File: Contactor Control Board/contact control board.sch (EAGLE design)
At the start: 29 parts, among them K1 DS2Y-S-DC5V, Q1 2n2222, Q3 2n2222, Q4 MOSFET-NCHANNELFQP30N06L, U1 LM393AN

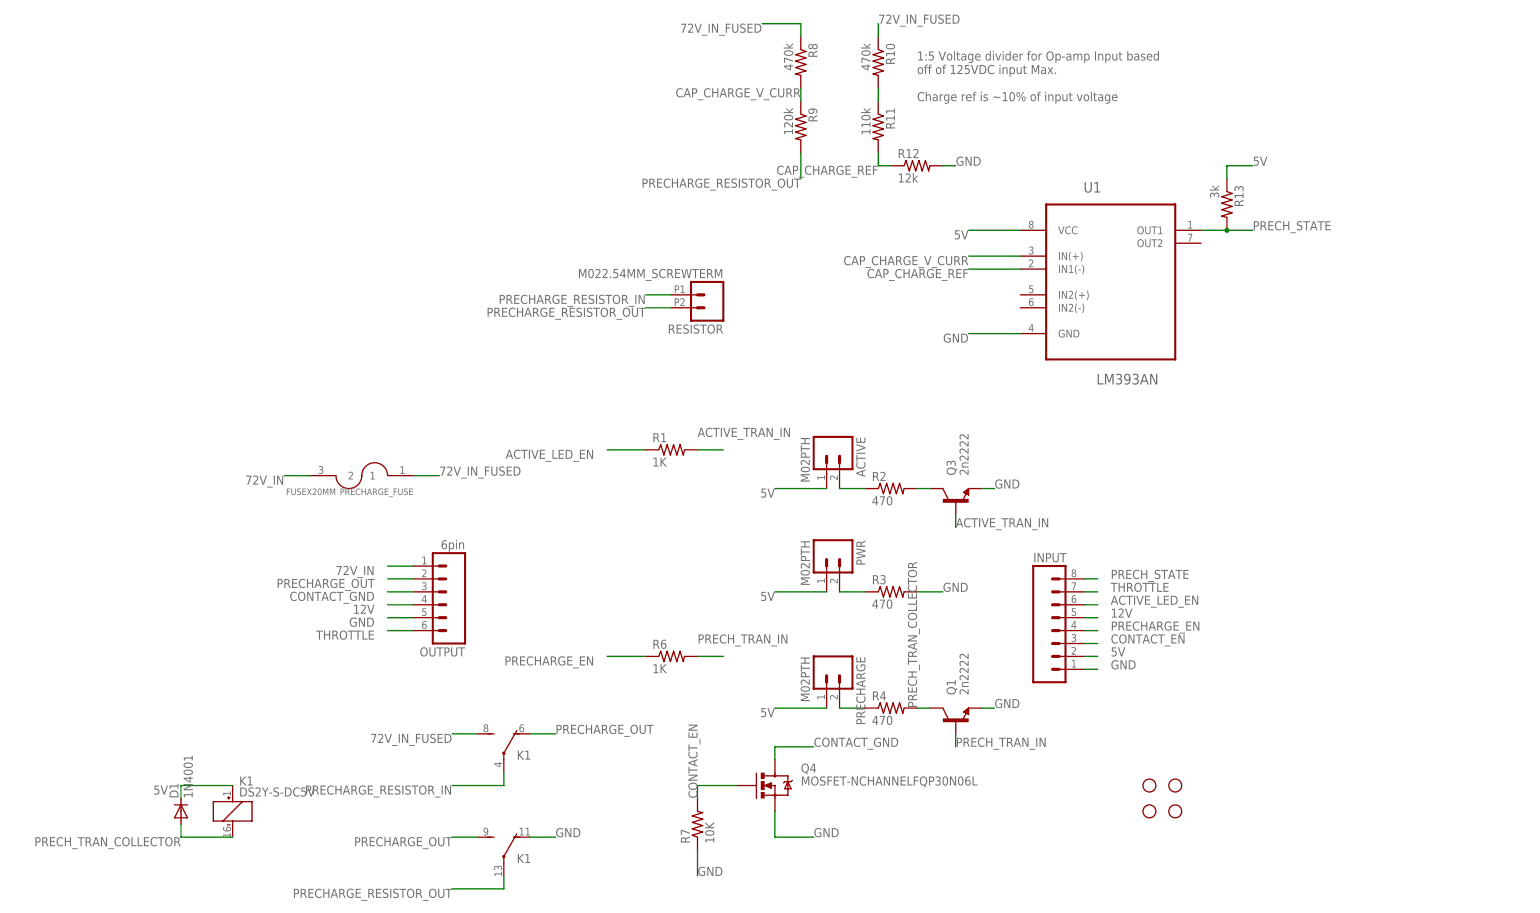
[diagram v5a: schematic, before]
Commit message: Simplified board by removing power LED pin, it's just run from 5V now.
Swapped pins in the voltage comparator to produce a HIGH output when the
capacitor voltage drops below the reference voltage (instead of vice
versa).
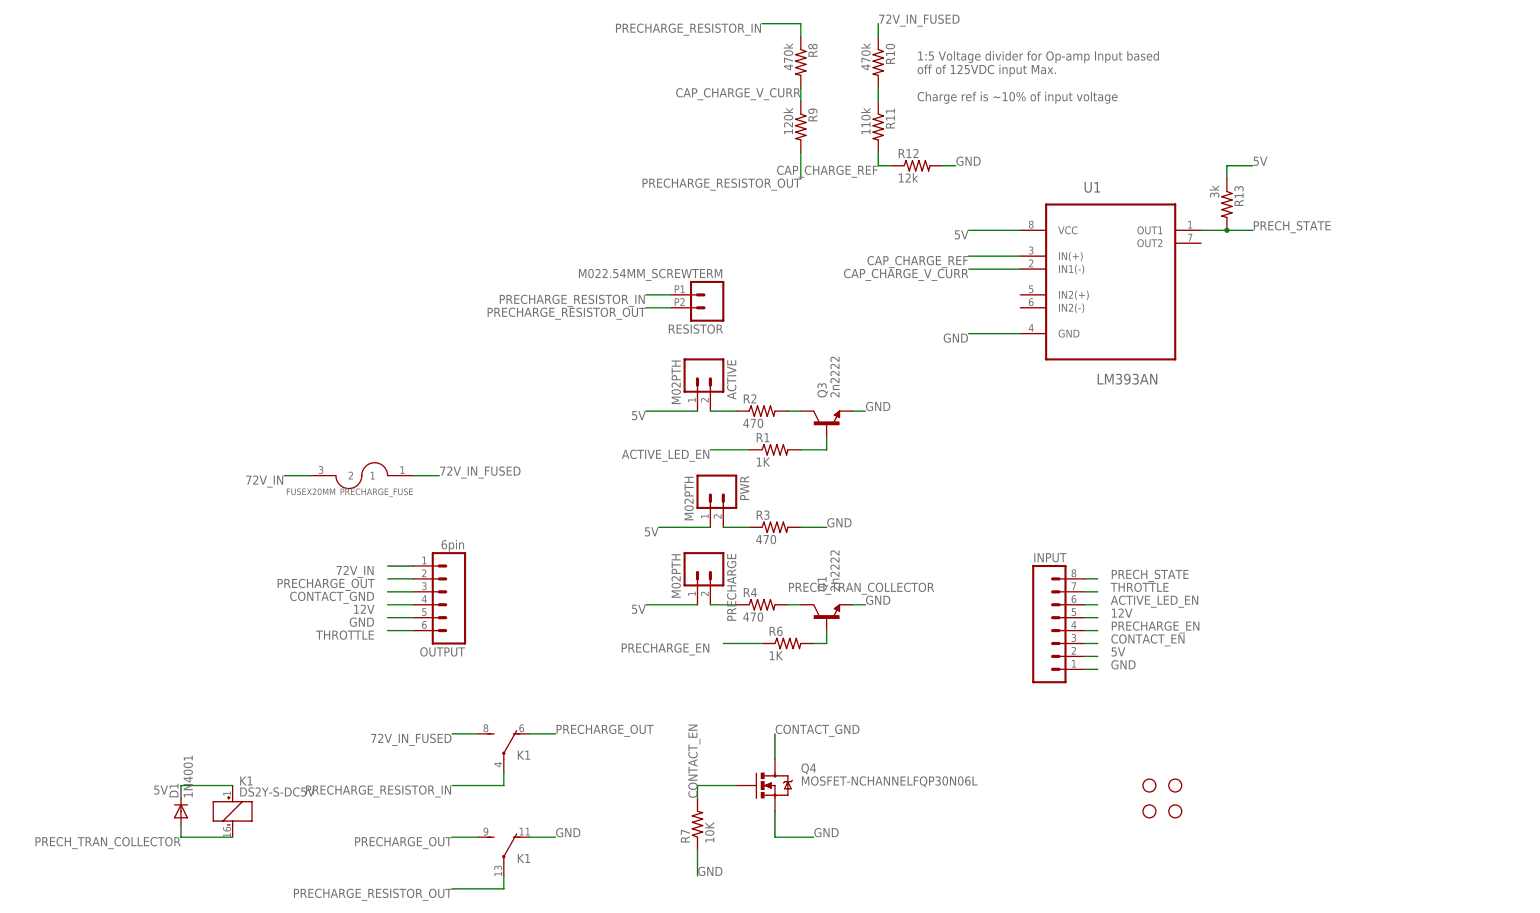
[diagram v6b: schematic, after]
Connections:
- net ACTIVE_TRAN_IN renamed N$2
- net 72V_IN_FUSED: no longer R8.1
- net CAP_CHARGE_REF: now also U1.IN(+); no longer U1.IN1(-)
- net CAP_CHARGE_V_CURR: now also U1.IN1(-); no longer U1.IN(+)
- net PRECHARGE_RESISTOR_IN: now also R8.1
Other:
- moved on the sheet: ACTIVE, PRECHARGE, PWR, Q1, Q3, R1, R2, R3, R4, R6
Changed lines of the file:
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@@
 </plain>
 <instances>
-<instance part="R1" gate="G$1" x="45.72" y="83.82"/>
-<instance part="R2" gate="G$1" x="88.9" y="76.2"/>
-<instance part="R3" gate="G$1" x="88.9" y="55.88"/>
-<instance part="R4" gate="G$1" x="88.9" y="33.02"/>
-<instance part="R6" gate="G$1" x="45.72" y="43.18"/>
+<instance part="R1" gate="G$1" x="66.04" y="83.82"/>
+<instance part="R2" gate="G$1" x="63.5" y="91.44"/>
+<instance part="R3" gate="G$1" x="66.04" y="68.58"/>
+<instance part="R4" gate="G$1" x="63.5" y="53.34"/>
+<instance part="R6" gate="G$1" x="68.58" y="45.72"/>
 <instance part="R7" gate="G$1" x="50.8" y="10.16" rot="R90"/>
 <instance part="Q4" gate="G$1" x="66.04" y="17.78"/>
@@
 <instance part="STANDOFF4" gate="G$1" x="139.7" y="12.7"/>
 <instance part="PRECHARGE_FUSE" gate="G$1" x="-15.24" y="78.74" rot="R180"/>
-<instance part="ACTIVE" gate="G$1" x="76.2" y="83.82" rot="R270"/>
-<instance part="PWR" gate="G$1" x="76.2" y="63.5" rot="R270"/>
-<instance part="PRECHARGE" gate="G$1" x="76.2" y="40.64" rot="R270"/>
-<instance part="Q1" gate="G$1" x="101.6" y="30.48" rot="R90"/>
-<instance part="Q3" gate="G$1" x="101.6" y="73.66" rot="R90"/>
+<instance part="ACTIVE" gate="G$1" x="50.8" y="99.06" rot="R270"/>
+<instance part="PWR" gate="G$1" x="53.34" y="76.2" rot="R270"/>
+<instance part="PRECHARGE" gate="G$1" x="50.8" y="60.96" rot="R270"/>
+<instance part="Q1" gate="G$1" x="76.2" y="50.8" rot="R90"/>
+<instance part="Q3" gate="G$1" x="76.2" y="88.9" rot="R90"/>
 <instance part="RESISTOR" gate="G$1" x="53.34" y="114.3" rot="R180"/>
 <instance part="R8" gate="G$1" x="71.12" y="160.02" rot="R270"/>
@@
 </segment>
 <segment>
-<wire x1="66.04" y1="76.2" x2="76.2" y2="76.2" width="0.2032" layer="91"/>
+<wire x1="40.64" y1="91.44" x2="50.8" y2="91.44" width="0.2032" layer="91"/>
 <pinref part="ACTIVE" gate="G$1" pin="1"/>
-<label x="66.04" y="76.2" size="1.778" layer="95" rot="R180"/>
+<label x="40.64" y="91.44" size="1.778" layer="95" rot="R180"/>
 </segment>
 <segment>
 <pinref part="PWR" gate="G$1" pin="1"/>
-<wire x1="76.2" y1="55.88" x2="66.04" y2="55.88" width="0.2032" layer="91"/>
-<label x="66.04" y="55.88" size="1.778" layer="95" rot="R180"/>
+<wire x1="53.34" y1="68.58" x2="43.18" y2="68.58" width="0.2032" layer="91"/>
+<label x="43.18" y="68.58" size="1.778" layer="95" rot="R180"/>
 </segment>
 <segment>
 <pinref part="PRECHARGE" gate="G$1" pin="1"/>
-<wire x1="76.2" y1="33.02" x2="66.04" y2="33.02" width="0.2032" layer="91"/>
-<label x="66.04" y="33.02" size="1.778" layer="95" rot="R180"/>
+<wire x1="50.8" y1="53.34" x2="40.64" y2="53.34" width="0.2032" layer="91"/>
+<label x="40.64" y="53.34" size="1.778" layer="95" rot="R180"/>
 </segment>
 <segment>
@@
 <segment>
 <pinref part="Q1" gate="G$1" pin="E"/>
-<wire x1="106.68" y1="33.02" x2="109.22" y2="33.02" width="0.2032" layer="91"/>
-<label x="109.22" y="33.02" size="1.778" layer="95"/>
+<wire x1="81.28" y1="53.34" x2="83.82" y2="53.34" width="0.2032" layer="91"/>
+<label x="83.82" y="53.34" size="1.778" layer="95"/>
 </segment>
 <segment>
 <pinref part="Q3" gate="G$1" pin="E"/>
-<wire x1="106.68" y1="76.2" x2="109.22" y2="76.2" width="0.2032" layer="91"/>
-<label x="109.22" y="76.2" size="1.778" layer="95"/>
+<wire x1="81.28" y1="91.44" x2="83.82" y2="91.44" width="0.2032" layer="91"/>
+<label x="83.82" y="91.44" size="1.778" layer="95"/>
 </segment>
 <segment>
@@
 <segment>
 <pinref part="R3" gate="G$1" pin="2"/>
-<wire x1="93.98" y1="55.88" x2="99.06" y2="55.88" width="0.2032" layer="91"/>
-<label x="99.06" y="55.88" size="1.778" layer="95"/>
+<wire x1="71.12" y1="68.58" x2="76.2" y2="68.58" width="0.2032" layer="91"/>
+<label x="76.2" y="68.58" size="1.778" layer="95"/>
 </segment>
 </net>
@@
 <segment>
 <pinref part="R6" gate="G$1" pin="1"/>
-<wire x1="40.64" y1="43.18" x2="33.02" y2="43.18" width="0.2032" layer="91"/>
-<label x="30.48" y="43.18" size="1.778" layer="95" rot="R180"/>
+<wire x1="63.5" y1="45.72" x2="55.88" y2="45.72" width="0.2032" layer="91"/>
+<label x="53.34" y="45.72" size="1.778" layer="95" rot="R180"/>
 </segment>
 <segment>
@@
 <segment>
 <pinref part="R1" gate="G$1" pin="1"/>
-<wire x1="40.64" y1="83.82" x2="33.02" y2="83.82" width="0.2032" layer="91"/>
-<label x="30.48" y="83.82" size="1.778" layer="95" rot="R180"/>
+<wire x1="60.96" y1="83.82" x2="53.34" y2="83.82" width="0.2032" layer="91"/>
+<label x="53.34" y="83.82" size="1.778" layer="95" rot="R180"/>
 </segment>
 </net>
@@
 <pinref part="R2" gate="G$1" pin="1"/>
 <pinref part="ACTIVE" gate="G$1" pin="2"/>
-<wire x1="78.74" y1="76.2" x2="83.82" y2="76.2" width="0.2032" layer="91"/>
+<wire x1="53.34" y1="91.44" x2="58.42" y2="91.44" width="0.2032" layer="91"/>
 </segment>
 </net>
@@
 <pinref part="R3" gate="G$1" pin="1"/>
 <pinref part="PWR" gate="G$1" pin="2"/>
-<wire x1="78.74" y1="55.88" x2="83.82" y2="55.88" width="0.2032" layer="91"/>
+<wire x1="55.88" y1="68.58" x2="60.96" y2="68.58" width="0.2032" layer="91"/>
 </segment>
 </net>
@@
 <pinref part="R4" gate="G$1" pin="1"/>
 <pinref part="PRECHARGE" gate="G$1" pin="2"/>
-<wire x1="78.74" y1="33.02" x2="83.82" y2="33.02" width="0.2032" layer="91"/>
+<wire x1="53.34" y1="53.34" x2="58.42" y2="53.34" width="0.2032" layer="91"/>
 </segment>
 </net>
@@
 </segment>
 <segment>
-<pinref part="R8" gate="G$1" pin="1"/>
-<wire x1="71.12" y1="165.1" x2="71.12" y2="167.64" width="0.2032" layer="91"/>
-<wire x1="71.12" y1="167.64" x2="63.5" y2="167.64" width="0.2032" layer="91"/>
-<label x="63.5" y="167.64" size="1.778" layer="95" rot="R180"/>
-</segment>
-<segment>
 <pinref part="K1" gate="2" pin="S"/>
 <wire x1="7.62" y1="27.94" x2="2.54" y2="27.94" width="0.2032" layer="91"/>
@@
 <segment>
 <pinref part="Q4" gate="G$1" pin="D"/>
-<wire x1="66.04" y1="22.86" x2="66.04" y2="25.4" width="0.2032" layer="91"/>
-<wire x1="66.04" y1="25.4" x2="73.66" y2="25.4" width="0.2032" layer="91"/>
-<label x="73.66" y="25.4" size="1.778" layer="95"/>
-</segment>
-</net>
-<net name="ACTIVE_TRAN_IN" class="0">
-<segment>
-<pinref part="R1" gate="G$1" pin="2"/>
-<wire x1="50.8" y1="83.82" x2="55.88" y2="83.82" width="0.2032" layer="91"/>
-<label x="50.8" y="86.36" size="1.778" layer="95"/>
-</segment>
-<segment>
-<wire x1="101.6" y1="71.12" x2="101.6" y2="68.58" width="0.2032" layer="91"/>
-<label x="101.6" y="68.58" size="1.778" layer="95"/>
-<pinref part="Q3" gate="G$1" pin="B"/>
-</segment>
-</net>
-<net name="PRECH_TRAN_IN" class="0">
-<segment>
-<pinref part="R6" gate="G$1" pin="2"/>
-<wire x1="50.8" y1="43.18" x2="55.88" y2="43.18" width="0.2032" layer="91"/>
-<label x="50.8" y="45.72" size="1.778" layer="95"/>
-</segment>
-<segment>
-<wire x1="101.6" y1="27.94" x2="101.6" y2="25.4" width="0.2032" layer="91"/>
-<label x="101.6" y="25.4" size="1.778" layer="95"/>
-<pinref part="Q1" gate="G$1" pin="B"/>
+<wire x1="66.04" y1="22.86" x2="66.04" y2="27.94" width="0.2032" layer="91"/>
+<label x="66.04" y="27.94" size="1.778" layer="95"/>
 </segment>
 </net>
@@
 <segment>
 <pinref part="R2" gate="G$1" pin="2"/>
-<wire x1="96.52" y1="76.2" x2="93.98" y2="76.2" width="0.1524" layer="91"/>
+<wire x1="71.12" y1="91.44" x2="68.58" y2="91.44" width="0.1524" layer="91"/>
 <pinref part="Q3" gate="G$1" pin="C"/>
 </segment>
@@
 <segment>
 <pinref part="R4" gate="G$1" pin="2"/>
-<wire x1="96.52" y1="33.02" x2="93.98" y2="33.02" width="0.1524" layer="91"/>
-<label x="93.98" y="33.02" size="1.778" layer="95" rot="R90"/>
+<wire x1="71.12" y1="53.34" x2="68.58" y2="53.34" width="0.1524" layer="91"/>
+<label x="68.58" y="55.88" size="1.778" layer="95"/>
 <pinref part="Q1" gate="G$1" pin="C"/>
 </segment>
@@
 <net name="CAP_CHARGE_REF" class="0">
 <segment>
-<wire x1="114.3" y1="119.38" x2="104.14" y2="119.38" width="0.2032" layer="91"/>
-<label x="104.14" y="119.38" size="1.778" layer="95" rot="R180"/>
-<pinref part="U1" gate="A" pin="IN1(-)"/>
-</segment>
-<segment>
 <pinref part="R11" gate="G$1" pin="2"/>
 <pinref part="R12" gate="G$1" pin="1"/>
@@
 <label x="86.36" y="139.7" size="1.778" layer="95" rot="R180"/>
 </segment>
+<segment>
+<wire x1="114.3" y1="121.92" x2="104.14" y2="121.92" width="0.2032" layer="91"/>
+<label x="104.14" y="121.92" size="1.778" layer="95" rot="R180"/>
+<pinref part="U1" gate="A" pin="IN(+)"/>
+</segment>
 </net>
 <net name="N$3" class="0">
@@
 </segment>
 <segment>
-<wire x1="114.3" y1="121.92" x2="104.14" y2="121.92" width="0.2032" layer="91"/>
-<label x="104.14" y="121.92" size="1.778" layer="95" rot="R180"/>
-<pinref part="U1" gate="A" pin="IN(+)"/>
+<wire x1="114.3" y1="119.38" x2="104.14" y2="119.38" width="0.2032" layer="91"/>
+<label x="104.14" y="119.38" size="1.778" layer="95" rot="R180"/>
+<pinref part="U1" gate="A" pin="IN1(-)"/>
 </segment>
 </net>
@@
 <label x="2.54" y="17.78" size="1.778" layer="95" rot="R180"/>
 </segment>
+<segment>
+<pinref part="R8" gate="G$1" pin="1"/>
+<wire x1="71.12" y1="165.1" x2="71.12" y2="167.64" width="0.2032" layer="91"/>
+<wire x1="71.12" y1="167.64" x2="63.5" y2="167.64" width="0.2032" layer="91"/>
+<label x="63.5" y="167.64" size="1.778" layer="95" rot="R180"/>
+</segment>
 </net>
 <net name="PRECHARGE_RESISTOR_OUT" class="0">
@@
 </segment>
 </net>
+<net name="N$2" class="0">
+<segment>
+<pinref part="R1" gate="G$1" pin="2"/>
+<pinref part="Q3" gate="G$1" pin="B"/>
+<wire x1="71.12" y1="83.82" x2="76.2" y2="83.82" width="0.2032" layer="91"/>
+<wire x1="76.2" y1="83.82" x2="76.2" y2="86.36" width="0.2032" layer="91"/>
+</segment>
+</net>
+<net name="PRECH_TRAN_IN" class="0">
+<segment>
+<pinref part="R6" gate="G$1" pin="2"/>
+<pinref part="Q1" gate="G$1" pin="B"/>
+<wire x1="73.66" y1="45.72" x2="76.2" y2="45.72" width="0.2032" layer="91"/>
+<wire x1="76.2" y1="45.72" x2="76.2" y2="48.26" width="0.2032" layer="91"/>
+</segment>
+</net>

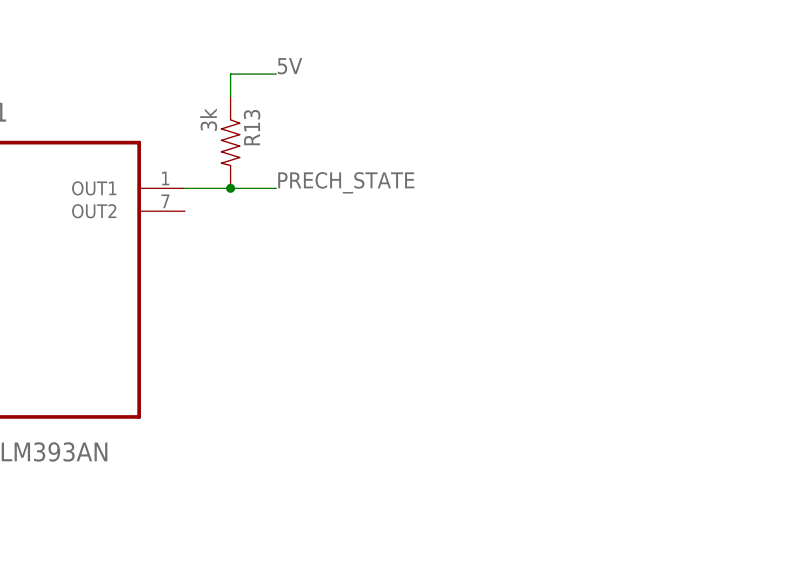
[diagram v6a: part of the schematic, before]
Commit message: Updating layout to 2"x3". Need to make smaller!
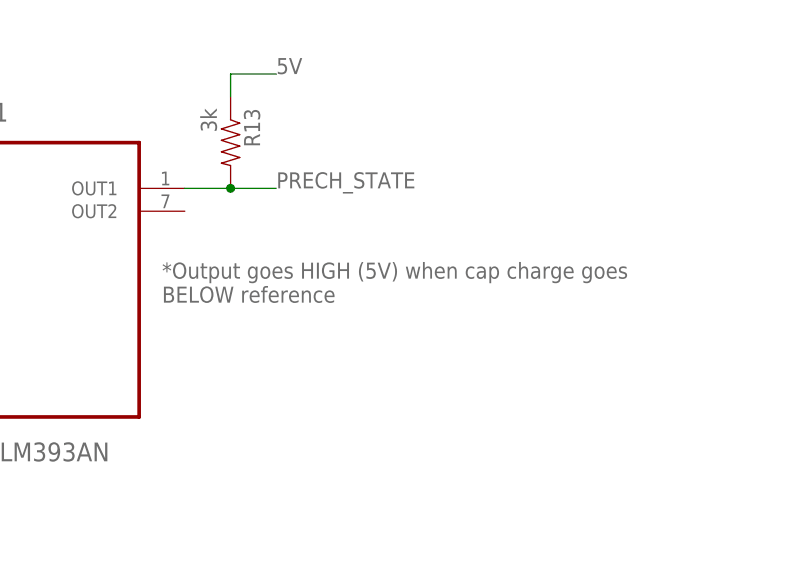
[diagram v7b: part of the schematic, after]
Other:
- note added: "*Output goes HIGH (5V) when cap charge goes BELOW reference"
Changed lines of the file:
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@@
 off of 125VDC input Max.
 Charge ref is ~10% of input voltage</text>
+<text x="147.32" y="114.3" size="1.778" layer="95">*Output goes HIGH (5V) when cap charge goes
+BELOW reference</text>
 </plain>
 <instances>
